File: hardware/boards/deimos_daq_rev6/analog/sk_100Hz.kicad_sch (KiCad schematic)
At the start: 9 parts, among them Q20001 MMBFJ113, Q20002 MMBFJ113, U20002 OPA196xDBV

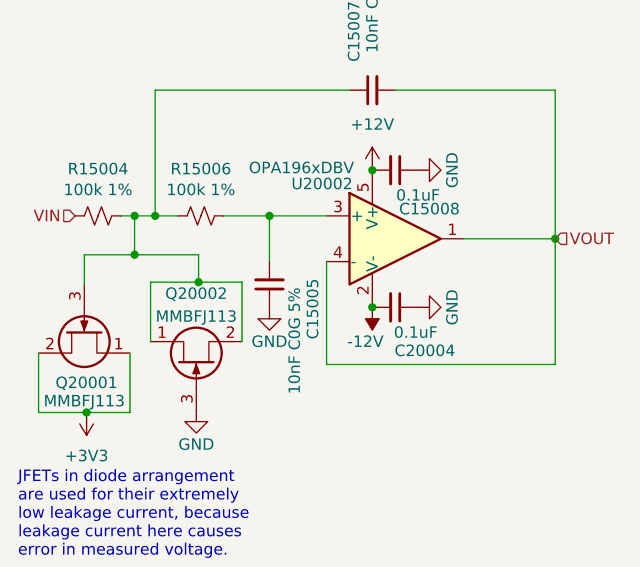
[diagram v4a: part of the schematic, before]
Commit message: exclude testpoints from BOM
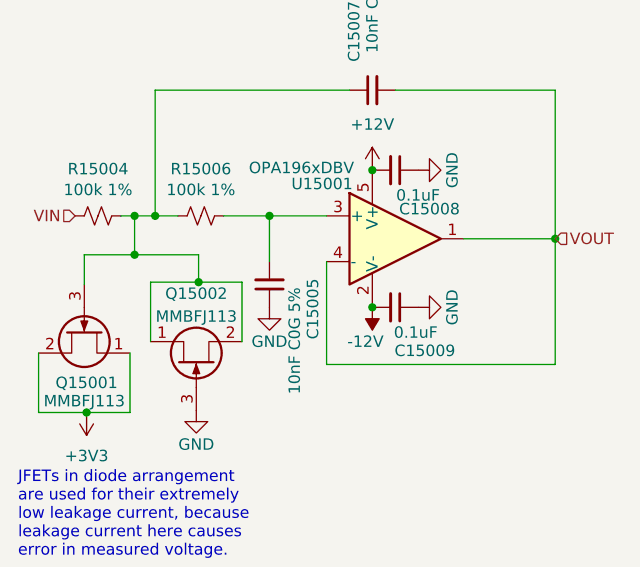
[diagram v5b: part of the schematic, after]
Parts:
- renumbered C20004 to C15009, Q20001 to Q15001, Q20002 to Q15002, U20002 to U15001
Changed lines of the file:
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@@
 		(dnp no)
 		(fields_autoplaced yes)
-		(property "Reference" "#PWR20002"
+		(property "Reference" "#PWR184"
 			(at 113.03 81.28 0)
 			(effects
@@
 		)
 		(instances
+			(project "analog_i"
+				(path "/5a60c4b1-b6cb-416e-8883-8291fa089b87/c2baf18d-2b19-4edb-98b3-535275ee271f/f31a785a-aa18-4b99-9461-7c34b37be0d7"
+					(reference "#PWR184")
+					(unit 1)
+				)
+				(path "/5a60c4b1-b6cb-416e-8883-8291fa089b87/c2baf18d-2b19-4edb-98b3-535275ee271f/ed60502d-2e6d-4293-85f2-5e967a3c42d8/63cb4c21-96ec-4930-8398-5e4d00a3dfaf"
+					(reference "#PWR323")
+					(unit 1)
+				)
+			)
 			(project ""
 				(path "/c241d083-1323-4b4a-a540-956d0afb7b72/f31a785a-aa18-4b99-9461-7c34b37be0d7"
@@
 		(on_board yes)
 		(dnp no)
-		(property "Reference" "Q20001"
+		(property "Reference" "Q15001"
 			(at 81.28 101.092 90)
 			(effects
@@
 		)
 		(instances
+			(project "analog_i"
+				(path "/5a60c4b1-b6cb-416e-8883-8291fa089b87/c2baf18d-2b19-4edb-98b3-535275ee271f/f31a785a-aa18-4b99-9461-7c34b37be0d7"
+					(reference "Q15001")
+					(unit 1)
+				)
+				(path "/5a60c4b1-b6cb-416e-8883-8291fa089b87/c2baf18d-2b19-4edb-98b3-535275ee271f/ed60502d-2e6d-4293-85f2-5e967a3c42d8/63cb4c21-96ec-4930-8398-5e4d00a3dfaf"
+					(reference "Q37001")
+					(unit 1)
+				)
+			)
 			(project "analog_frontend_panel"
 				(path "/c241d083-1323-4b4a-a540-956d0afb7b72/f31a785a-aa18-4b99-9461-7c34b37be0d7"
@@
 		(on_board yes)
 		(dnp no)
-		(property "Reference" "#PWR20007"
+		(property "Reference" "#PWR179"
 			(at 93.472 110.49 0)
 			(effects
@@
 		)
 		(instances
+			(project "analog_i"
+				(path "/5a60c4b1-b6cb-416e-8883-8291fa089b87/c2baf18d-2b19-4edb-98b3-535275ee271f/f31a785a-aa18-4b99-9461-7c34b37be0d7"
+					(reference "#PWR179")
+					(unit 1)
+				)
+				(path "/5a60c4b1-b6cb-416e-8883-8291fa089b87/c2baf18d-2b19-4edb-98b3-535275ee271f/ed60502d-2e6d-4293-85f2-5e967a3c42d8/63cb4c21-96ec-4930-8398-5e4d00a3dfaf"
+					(reference "#PWR316")
+					(unit 1)
+				)
+			)
 			(project "analog_frontend_panel"
 				(path "/c241d083-1323-4b4a-a540-956d0afb7b72/f31a785a-aa18-4b99-9461-7c34b37be0d7"
@@
 		(on_board yes)
 		(dnp no)
-		(property "Reference" "C20004"
+		(property "Reference" "C15009"
 			(at 118.872 97.536 90)
 			(effects
@@
 		)
 		(instances
+			(project "analog_i"
+				(path "/5a60c4b1-b6cb-416e-8883-8291fa089b87/c2baf18d-2b19-4edb-98b3-535275ee271f/f31a785a-aa18-4b99-9461-7c34b37be0d7"
+					(reference "C15009")
+					(unit 1)
+				)
+				(path "/5a60c4b1-b6cb-416e-8883-8291fa089b87/c2baf18d-2b19-4edb-98b3-535275ee271f/ed60502d-2e6d-4293-85f2-5e967a3c42d8/63cb4c21-96ec-4930-8398-5e4d00a3dfaf"
+					(reference "C37004")
+					(unit 1)
+				)
+			)
 			(project "analog_frontend_panel"
 				(path "/c241d083-1323-4b4a-a540-956d0afb7b72/f31a785a-aa18-4b99-9461-7c34b37be0d7"
@@
 		(on_board yes)
 		(dnp no)
-		(property "Reference" "U20002"
+		(property "Reference" "U15001"
 			(at 107.442 78.994 0)
 			(effects
@@
 		)
 		(instances
+			(project "analog_i"
+				(path "/5a60c4b1-b6cb-416e-8883-8291fa089b87/c2baf18d-2b19-4edb-98b3-535275ee271f/f31a785a-aa18-4b99-9461-7c34b37be0d7"
+					(reference "U15001")
+					(unit 1)
+				)
+				(path "/5a60c4b1-b6cb-416e-8883-8291fa089b87/c2baf18d-2b19-4edb-98b3-535275ee271f/ed60502d-2e6d-4293-85f2-5e967a3c42d8/63cb4c21-96ec-4930-8398-5e4d00a3dfaf"
+					(reference "U37001")
+					(unit 1)
+				)
+			)
 			(project ""
 				(path "/c241d083-1323-4b4a-a540-956d0afb7b72/f31a785a-aa18-4b99-9461-7c34b37be0d7"
@@
 		(on_board yes)
 		(dnp no)
-		(property "Reference" "#PWR20006"
+		(property "Reference" "#PWR181"
 			(at 113.03 88.9 0)
 			(effects
@@
 		)
 		(instances
+			(project "analog_i"
+				(path "/5a60c4b1-b6cb-416e-8883-8291fa089b87/c2baf18d-2b19-4edb-98b3-535275ee271f/f31a785a-aa18-4b99-9461-7c34b37be0d7"
+					(reference "#PWR181")
+					(unit 1)
+				)
+				(path "/5a60c4b1-b6cb-416e-8883-8291fa089b87/c2baf18d-2b19-4edb-98b3-535275ee271f/ed60502d-2e6d-4293-85f2-5e967a3c42d8/63cb4c21-96ec-4930-8398-5e4d00a3dfaf"
+					(reference "#PWR321")
+					(unit 1)
+				)
+			)
 			(project ""
 				(path "/c241d083-1323-4b4a-a540-956d0afb7b72/f31a785a-aa18-4b99-9461-7c34b37be0d7"
@@
 		(dnp no)
 		(fields_autoplaced yes)
-		(property "Reference" "#PWR20005"
+		(property "Reference" "#PWR180"
 			(at 81.28 100.584 0)
 			(effects
@@
 		)
 		(instances
+			(project "analog_i"
+				(path "/5a60c4b1-b6cb-416e-8883-8291fa089b87/c2baf18d-2b19-4edb-98b3-535275ee271f/f31a785a-aa18-4b99-9461-7c34b37be0d7"
+					(reference "#PWR180")
+					(unit 1)
+				)
+				(path "/5a60c4b1-b6cb-416e-8883-8291fa089b87/c2baf18d-2b19-4edb-98b3-535275ee271f/ed60502d-2e6d-4293-85f2-5e967a3c42d8/63cb4c21-96ec-4930-8398-5e4d00a3dfaf"
+					(reference "#PWR318")
+					(unit 1)
+				)
+			)
 			(project ""
 				(path "/c241d083-1323-4b4a-a540-956d0afb7b72/f31a785a-aa18-4b99-9461-7c34b37be0d7"
@@
 		(on_board yes)
 		(dnp no)
-		(property "Reference" "Q20002"
+		(property "Reference" "Q15002"
 			(at 93.472 91.186 90)
 			(effects
@@
 		)
 		(instances
+			(project "analog_i"
+				(path "/5a60c4b1-b6cb-416e-8883-8291fa089b87/c2baf18d-2b19-4edb-98b3-535275ee271f/f31a785a-aa18-4b99-9461-7c34b37be0d7"
+					(reference "Q15002")
+					(unit 1)
+				)
+				(path "/5a60c4b1-b6cb-416e-8883-8291fa089b87/c2baf18d-2b19-4edb-98b3-535275ee271f/ed60502d-2e6d-4293-85f2-5e967a3c42d8/63cb4c21-96ec-4930-8398-5e4d00a3dfaf"
+					(reference "Q37002")
+					(unit 1)
+				)
+			)
 			(project "analog_frontend_panel"
 				(path "/c241d083-1323-4b4a-a540-956d0afb7b72/f31a785a-aa18-4b99-9461-7c34b37be0d7"
@@
 		(on_board yes)
 		(dnp no)
-		(property "Reference" "#PWR20003"
+		(property "Reference" "#PWR182"
 			(at 124.46 92.71 0)
 			(effects
@@
 		)
 		(instances
+			(project "analog_i"
+				(path "/5a60c4b1-b6cb-416e-8883-8291fa089b87/c2baf18d-2b19-4edb-98b3-535275ee271f/f31a785a-aa18-4b99-9461-7c34b37be0d7"
+					(reference "#PWR182")
+					(unit 1)
+				)
+				(path "/5a60c4b1-b6cb-416e-8883-8291fa089b87/c2baf18d-2b19-4edb-98b3-535275ee271f/ed60502d-2e6d-4293-85f2-5e967a3c42d8/63cb4c21-96ec-4930-8398-5e4d00a3dfaf"
+					(reference "#PWR322")
+					(unit 1)
+				)
+			)
 			(project "analog_frontend_panel"
 				(path "/c241d083-1323-4b4a-a540-956d0afb7b72/f31a785a-aa18-4b99-9461-7c34b37be0d7"
